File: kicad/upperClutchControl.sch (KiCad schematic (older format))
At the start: 12 parts

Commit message: KICAD: Guardar cambios sch de los controles de los cluches y freno
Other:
- note added: "Blanco/Verde"
- note added: "Verde"
- note added: "upperClutchControl"
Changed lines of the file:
@@
 Sheet 16 22
 Title "Mainet-mega -- upperClutchControl"
-Date "2021-04-07"
+Date "2021-07-09"
 Rev "1.0"
 Comp "Tovenca"
@@
 Text Label 8000 4700 0    50   ~ 0
 0V
+Text Notes 8650 3450 0    50   ~ 0
+Verde
+Text Notes 8650 3650 0    50   ~ 0
+Blanco/Verde
+Text Notes 7450 3550 0    50   ~ 0
+upperClutchControl
 $EndSCHEMATC

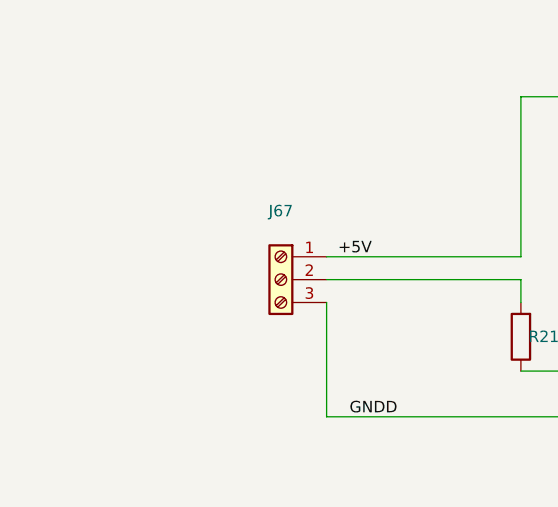
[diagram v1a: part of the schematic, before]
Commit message: KICAD: Agregar cvambios .sch controles tarjetas MP
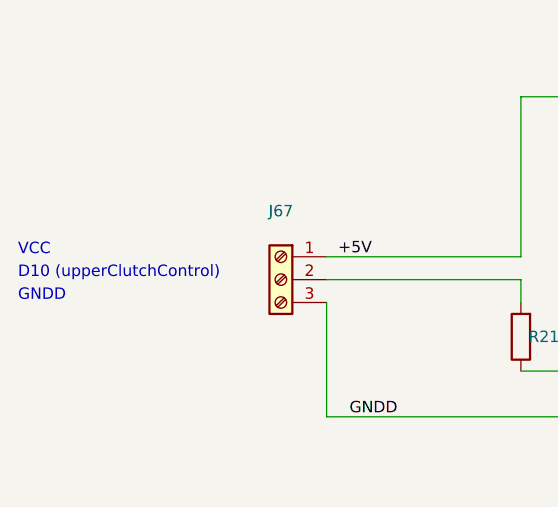
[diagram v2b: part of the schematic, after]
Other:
- note added: "D10 (upperClutchControl)"
- note added: "GNDD"
- note added: "VCC"
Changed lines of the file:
@@
 Sheet 16 22
 Title "Mainet-mega -- upperClutchControl"
-Date "2021-07-09"
+Date "2021-07-13"
 Rev "1.0"
 Comp "Tovenca"
@@
 Text Notes 7450 3550 0    50   ~ 0
 upperClutchControl
+Text Notes 2850 3800 0    50   ~ 0
+D10 (upperClutchControl)
+Text Notes 2850 3900 0    50   ~ 0
+GNDD
+Text Notes 2850 3700 0    50   ~ 0
+VCC
 $EndSCHEMATC
